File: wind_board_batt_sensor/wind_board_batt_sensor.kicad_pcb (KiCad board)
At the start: 2 copper layers, 82.4 x 23.5 mm, 40 parts, among them J1 Batt +, J2 Batt -, J3 Sys +, J4 Sys -, J5 Conn_01x03_Socket, J6 Conn_01x02_Socket, U1 MAX17263xxTE, U2 PTSM82903SISB2R, U3 ATtiny402-SS

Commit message: update bom
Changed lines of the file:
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@@
 			(plot_on_all_layers_selection 0x00000000_00000000_00000000_00000000)
 			(disableapertmacros no)
-			(usegerberextensions no)
+			(usegerberextensions yes)
 			(usegerberattributes yes)
 			(usegerberadvancedattributes yes)
@@
 			(outputformat 1)
 			(mirror no)
-			(drillshape 1)
+			(drillshape 0)
 			(scaleselection 1)
-			(outputdirectory "")
+			(outputdirectory "gerber/")
 		)
 	)
@@
 			(at 0 -2.38 180)
 			(layer "F.SilkS")
+			(hide yes)
 			(effects
 				(font
@@
 			(layers "*.Cu" "*.Mask")
 			(remove_unused_layers no)
+			(net 1 "~")
 			(zone_connect 2)
 		)
@@
 		(layer "F.Cu")
 		(net 18)
-	)
-	(segment
-		(start 156.8125 109.5625)
-		(end 156.8 109.55)
-		(width 0.3)
-		(layer "F.Cu")
-		(net 18)

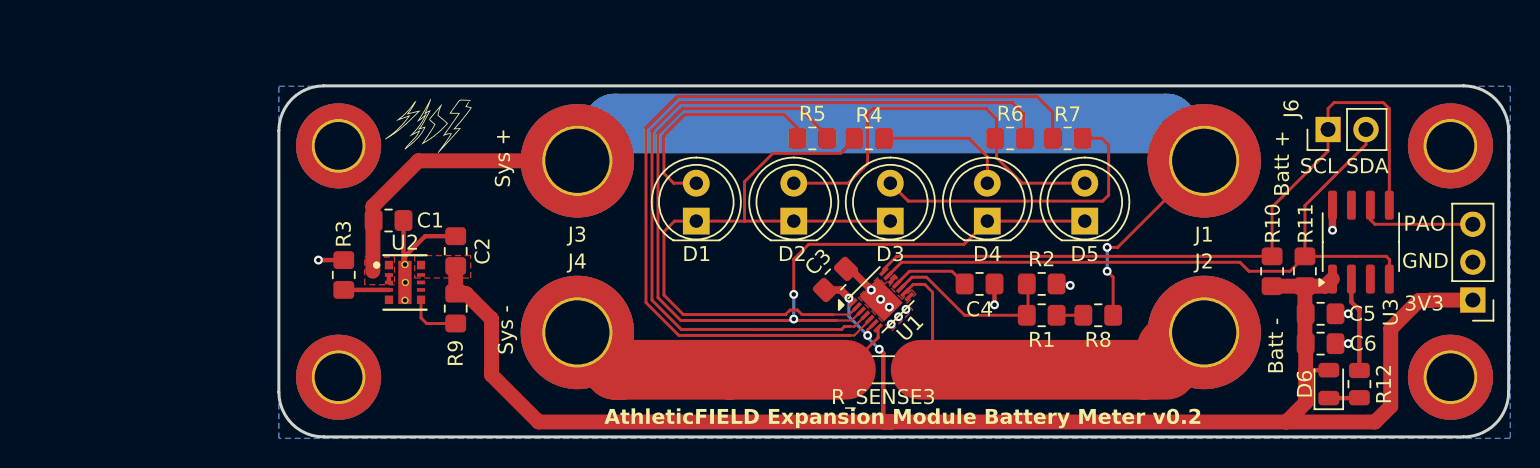
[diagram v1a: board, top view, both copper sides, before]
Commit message: new power supply
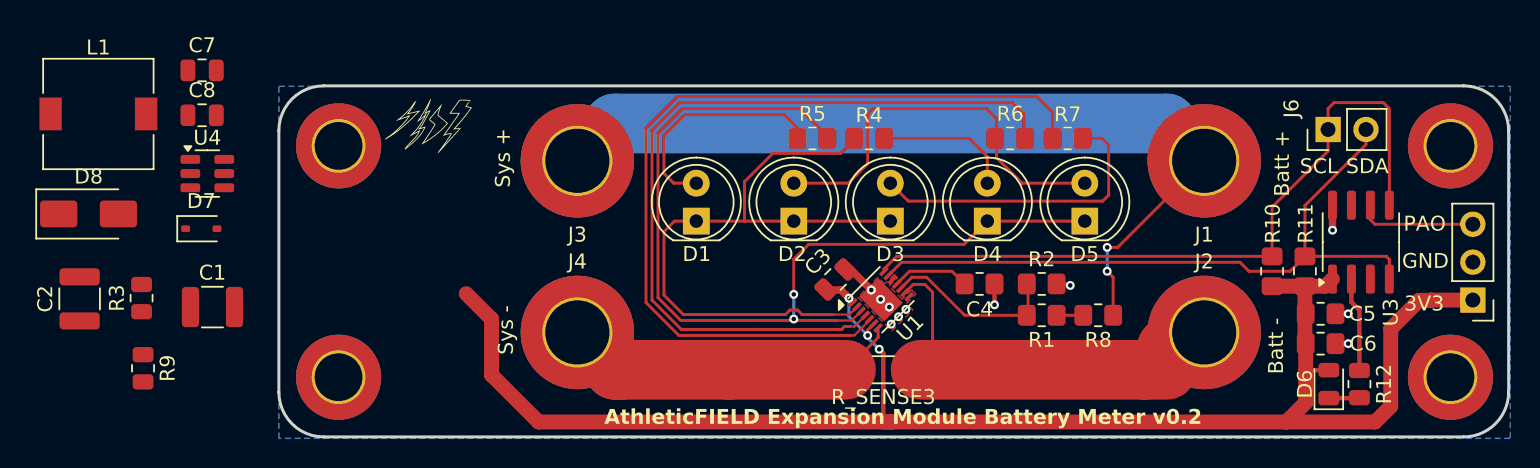
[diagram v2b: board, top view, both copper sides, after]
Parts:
- removed U2: PTSM82903SISB2R, TPSM82903:SIS0011A-MFG
- added C7: 10uF, Capacitor_SMD:C_0805_2012Metric, F.Cu at (82.9, 88.9)
- added C8: 10uF, Capacitor_SMD:C_0805_2012Metric, F.Cu at (82.9, 92.0)
- added D7: 1N4148WS-7-F, Diode_SMD:D_SOD-323, F.Cu at (82.8, 99.5)
- added D8: B1100-13-F, Diode_SMD:D_SMA, F.Cu at (75.2, 98.6)
- added L1: 15uH, Inductor_SMD:L_7.3x7.3_H4.5, F.Cu at (75.9, 91.9)
- added U4: MCP16331x-xCH, Package_TO_SOT_SMD:SOT-23-6, F.Cu at (83.2, 95.9)
- C1: value 10uF -> 10uf; footprint Resistor_SMD:R_0805_2012Metric_Pad1.20x1.40mm_HandSolder -> Capacitor_SMD:C_1210_3225Metric
- C2: value 22uF -> 10uf; footprint Resistor_SMD:R_0805_2012Metric_Pad1.20x1.40mm_HandSolder -> Capacitor_SMD:C_1210_3225Metric
- C3: value 100 nF -> 100nF; footprint Resistor_SMD:R_0805_2012Metric_Pad1.20x1.40mm_HandSolder -> Capacitor_SMD:C_0805_2012Metric
- R3: value 26.1k -> 31.6K - 1%; footprint Resistor_SMD:R_0805_2012Metric_Pad1.20x1.40mm_HandSolder -> Resistor_SMD:R_0805_2012Metric
- R9: value 10K -> 10K - 1%; footprint Resistor_SMD:R_0805_2012Metric_Pad1.20x1.40mm_HandSolder -> Resistor_SMD:R_0805_2012Metric
- moved C2 25.4 mm to (74.7, 104.2)
- moved R9 21.3 mm to (78.9, 108.9)
- moved R3 13.6 mm to (78.8, 104.2)
- moved C1 13.1 mm to (83.5, 104.8)
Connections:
- C1 pad 1: Net-(J1-Pin_1) -> +12V
- C2 pad 1: +3.3V -> +12V
- C3 pad 1: +3.3V -> Net-(D7-K)
- C3 pad 2: ~ -> Net-(D8-K)
- J1 pad 1: Net-(J1-Pin_1) -> +12V
- J3 pad 1: Net-(J1-Pin_1) -> +12V
- R3 pad 1: Net-(U2-MODE_S-CONF) -> +3.3V
- R3 pad 2: ~ -> Net-(U4-V_{FB})
- R8 pad 1: Net-(J1-Pin_1) -> +12V
- R9 pad 1: +3.3V -> Net-(U4-V_{FB})
- R9 pad 2: Net-(U2-PG) -> ~
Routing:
- net Net-(J1-Pin_1): track 77.9 -> 0.00 mm, vias 2 -> 0
- net +12V: track 0.00 -> 58.1 mm, vias 0 -> 2
- net ~: track 47.2 -> 38.0 mm, vias 12 -> 11
- net Net-(U2-PG): track 3.69 -> 0.00 mm
- net Net-(U2-MODE_S-CONF): track 3.03 -> 0.00 mm
- net +3.3V: track 110.6 -> 108.1 mm
- removed copper zone on F.Cu, net +3.3V
- removed copper zone on F.Cu, net Net-(J1-Pin_1)

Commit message: add new power supply
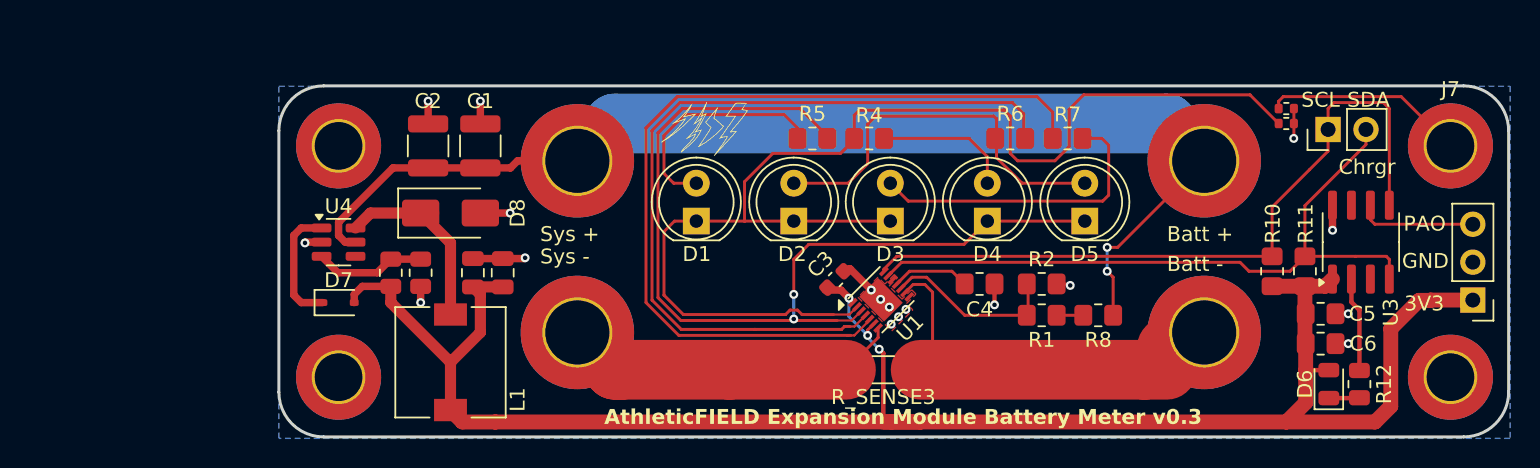
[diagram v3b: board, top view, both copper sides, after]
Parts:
- removed the REF** at (166.5, 94.0)
- added J7: PB Input, MountingHole:MountingHole_3.2mm_M3_ISO7380_Pad_TopBottom, F.Cu at (166.5, 94.0)
- added R13: 100K, Resistor_SMD:R_0402_1005Metric, F.Cu at (155.5, 91.5)
- added R14: 100K, Resistor_SMD:R_0402_1005Metric, F.Cu at (155.5, 92.5)
- C3: footprint Capacitor_SMD:C_0805_2012Metric -> Capacitor_SMD:C_0603_1608Metric
- moved L1 28.9 mm to (99.5, 108.5), turned to -90 degrees
- moved C2 25.5 mm to (98.0, 94.0)
- moved C7 24.3 mm to (103.0, 102.5), turned to 90 degrees
- moved D8 24.3 mm to (99.5, 98.5)
- moved C8 21.0 mm to (101.0, 102.5), turned to 90 degrees
- moved C1 20.9 mm to (101.5, 94.0), turned to 90 degrees
- moved R9 19.7 mm to (97.5, 102.5)
- moved G*** 18.5 mm to (116.5, 93.0)
- moved R3 16.8 mm to (95.5, 102.5)
- moved D7 10.4 mm to (92.0, 104.5)
- moved U4 9.92 mm to (92.0, 100.5)
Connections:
- C3 pad 1: Net-(D7-K) -> +3.3V
- C3 pad 2: Net-(D8-K) -> ~
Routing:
- net Net-(D1-K): track 44.9 -> 82.0 mm
- net +12V: track 58.1 -> 78.0 mm
- net +3.3V: track 108.1 -> 126.9 mm
- net Net-(J7-Pin_1): track 0.00 -> 13.5 mm
- net Net-(D8-K): track 0.00 -> 13.4 mm
- net ~: track 38.0 -> 50.8 mm, vias 11 -> 18
- net Net-(D7-K): track 0.00 -> 8.23 mm
- net Net-(U4-V_{FB}): track 0.00 -> 7.47 mm
- net Net-(D2-A): track 27.1 -> 26.3 mm
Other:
- board text added: "AthleticFIELD Expansion Module Battery Meter v0.3"
- board text added: "Chrgr"
- board text removed: "AthleticFIELD Expansion Module Battery Meter v0.2"

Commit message: new regulator
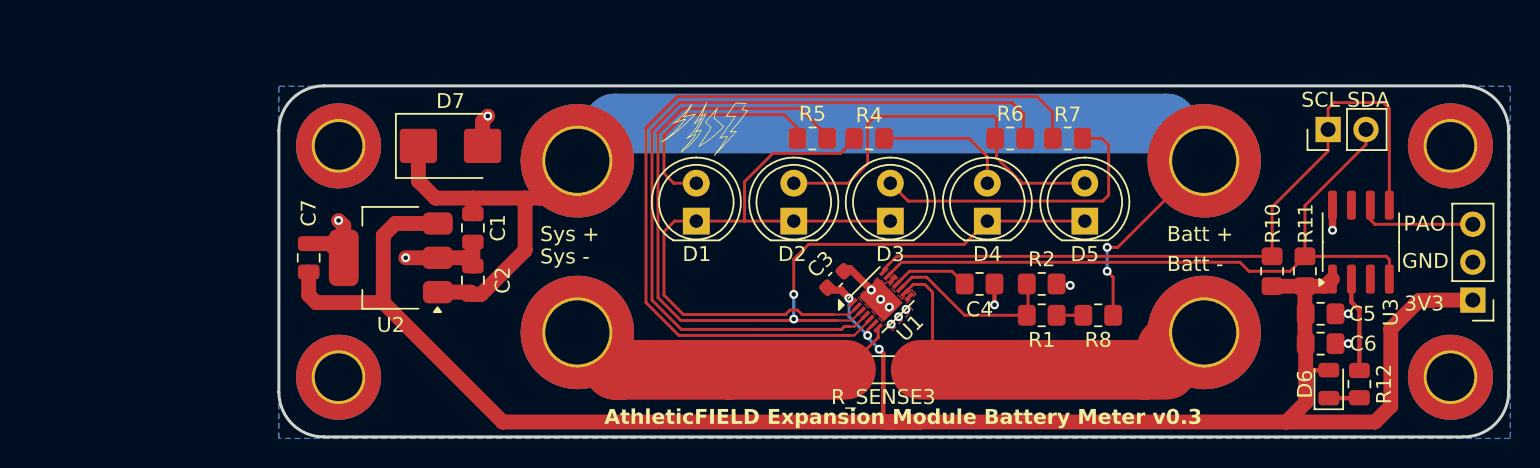
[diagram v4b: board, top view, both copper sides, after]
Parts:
- removed C8: 10uF, Capacitor_SMD:C_0805_2012Metric
- removed D8: B1100-13-F, Diode_SMD:D_SMA
- removed J7: PB Input, MountingHole:MountingHole_3.2mm_M3_ISO7380_Pad_TopBottom
- removed L1: 15uH, Inductor_SMD:L_7.3x7.3_H4.5
- removed R13, R14: 100K, Resistor_SMD:R_0402_1005Metric
- removed R3: 31.6K - 1%, Resistor_SMD:R_0805_2012Metric
- removed R9: 10K - 1%, Resistor_SMD:R_0805_2012Metric
- removed U4: MCP16331x-xCH, Package_TO_SOT_SMD:SOT-23-6
- added REF**: MountingHole_3.2mm_M3_ISO7380_Pad_TopBottom, MountingHole:MountingHole_3.2mm_M3_ISO7380_Pad_TopBottom, F.Cu at (166.5, 94.0)
- added U2: TLE42744GS V33, Package_TO_SOT_SMD:SOT-223, F.Cu at (95.5, 101.5)
- C1: value 10uf -> 10uF; footprint Capacitor_SMD:C_1210_3225Metric -> Capacitor_SMD:C_0805_2012Metric
- C2: value 10uf -> 100nF; footprint Capacitor_SMD:C_1210_3225Metric -> Capacitor_SMD:C_0805_2012Metric
- C7: value 10uF -> 22uF
- D7: value 1N4148WS-7-F -> SMBJ18A; footprint Diode_SMD:D_SOD-323 -> Diode_SMD:D_SMB
- moved C7 13.0 mm to (90.0, 101.5)
- moved D7 12.9 mm to (99.5, 94.0)
- moved C2 9.49 mm to (101.0, 103.0)
- moved C1 5.52 mm to (101.0, 99.5), turned to -90 degrees
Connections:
- D7 pad 1: Net-(D7-K) -> +12V
- D7 pad 2: +3.3V -> ~
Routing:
- net Net-(D1-K): track 82.0 -> 44.9 mm
- net Net-(J7-Pin_1): track 13.5 -> 0.00 mm
- net Net-(D8-K): track 13.4 -> 0.00 mm
- net Net-(D7-K): track 8.23 -> 0.00 mm
- net Net-(U4-V_{FB}): track 7.47 -> 0.00 mm
- net +12V: track 78.0 -> 84.3 mm
- net ~: track 50.8 -> 51.8 mm, vias 18 -> 14
- net +3.3V: track 126.9 -> 127.9 mm
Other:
- board text removed: "Chrgr"

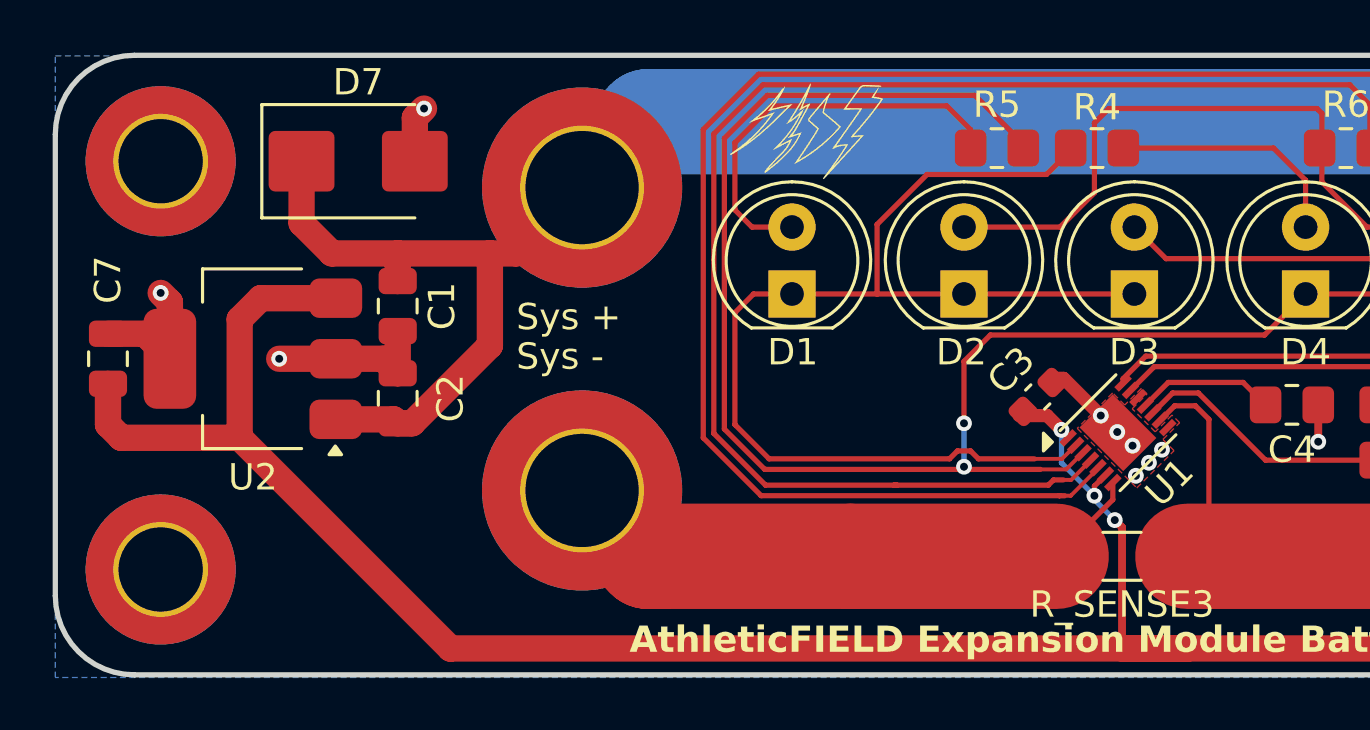
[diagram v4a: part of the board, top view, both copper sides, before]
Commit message: update layout around PSU
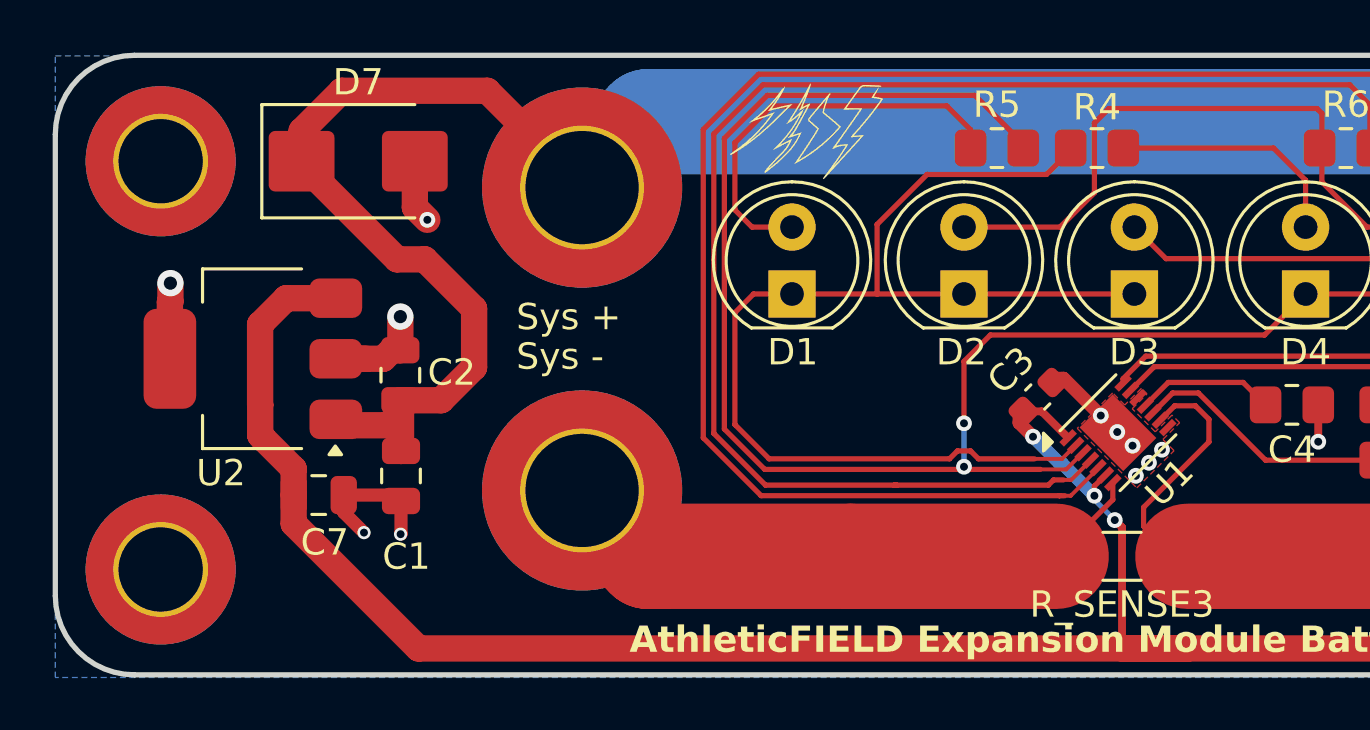
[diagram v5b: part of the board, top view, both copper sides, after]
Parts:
- moved C7 9.53 mm to (98.0, 106.7), turned to 0 degrees
- moved C1 6.45 mm to (101.1, 106.0)
- moved C2 0.88 mm to (101.1, 102.1)
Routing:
- net +12V: track 84.3 -> 92.1 mm
- net +3.3V: track 127.9 -> 122.2 mm
- net ~: track 51.8 -> 55.7 mm, vias 14 -> 16

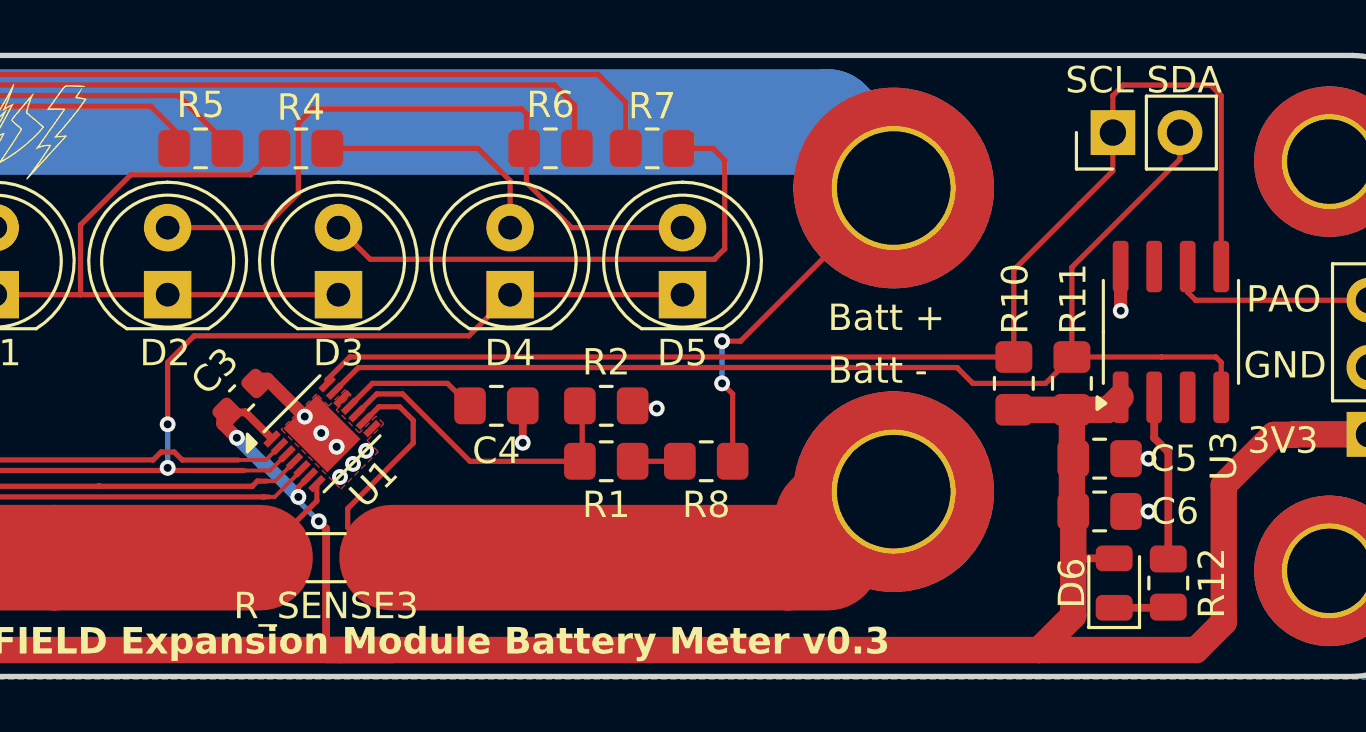
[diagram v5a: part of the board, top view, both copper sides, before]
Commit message: new power supply
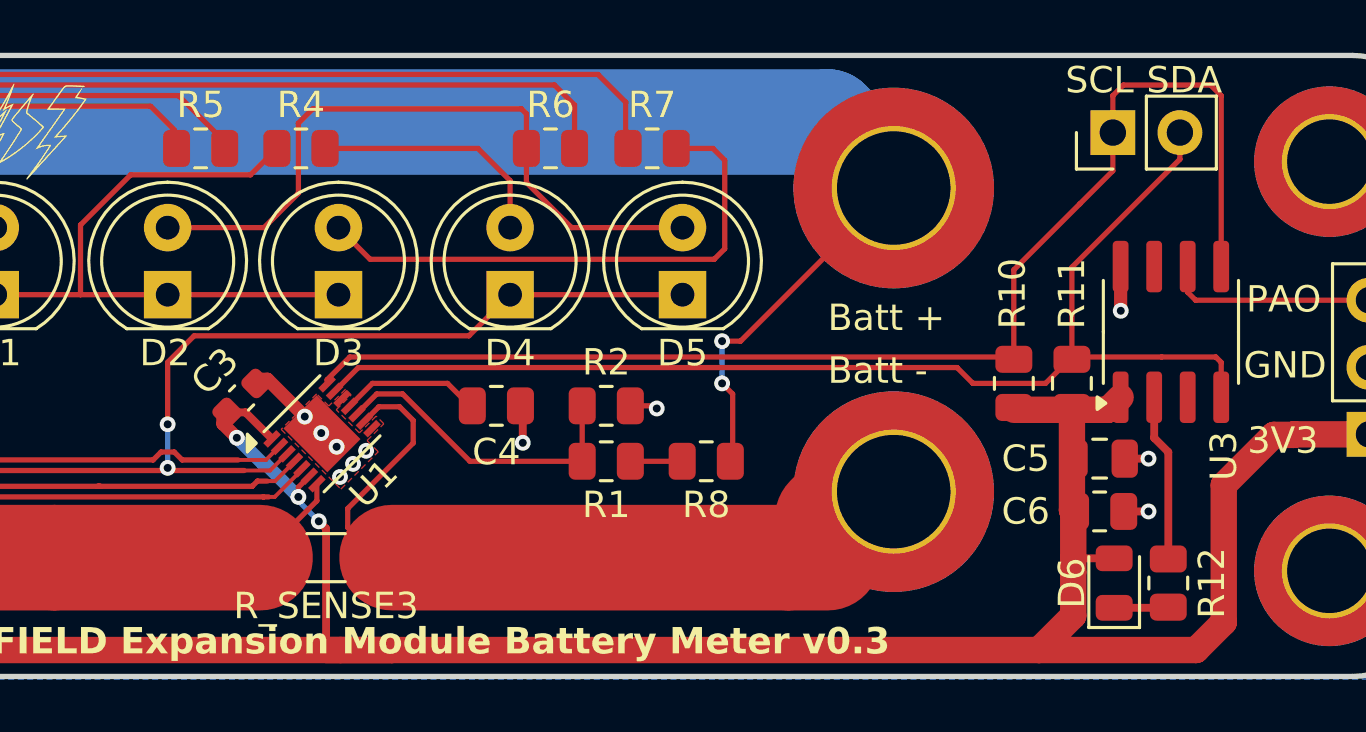
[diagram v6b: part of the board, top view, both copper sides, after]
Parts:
- C4, C6, R1, R10, R11, R2, R4, R5, R6, R7, R8: footprint Resistor_SMD:R_0805_2012Metric_Pad1.20x1.40mm_HandSolder -> Resistor_SMD:R_0805_2012Metric
- C5: footprint Resistor_SMD:R_0805_2012Metric_Pad1.20x1.40mm_HandSolder -> Capacitor_SMD:C_0805_2012Metric
- R_SENSE3: footprint Resistor_SMD:R_1206_3216Metric_Pad1.30x1.75mm_HandSolder -> Resistor_SMD:R_1206_3216Metric
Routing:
- net ~: track 55.7 -> 54.6 mm
